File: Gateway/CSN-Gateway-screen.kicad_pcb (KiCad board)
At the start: 2 copper layers, 32 x 58 mm, 27 parts, among them IC2 FT232RL, P1 USB_MINI, P2 CONN_01X12, P4 CONN_OLED_SCREEN, SW1 SW_PUSH, SW2 SW_PUSH

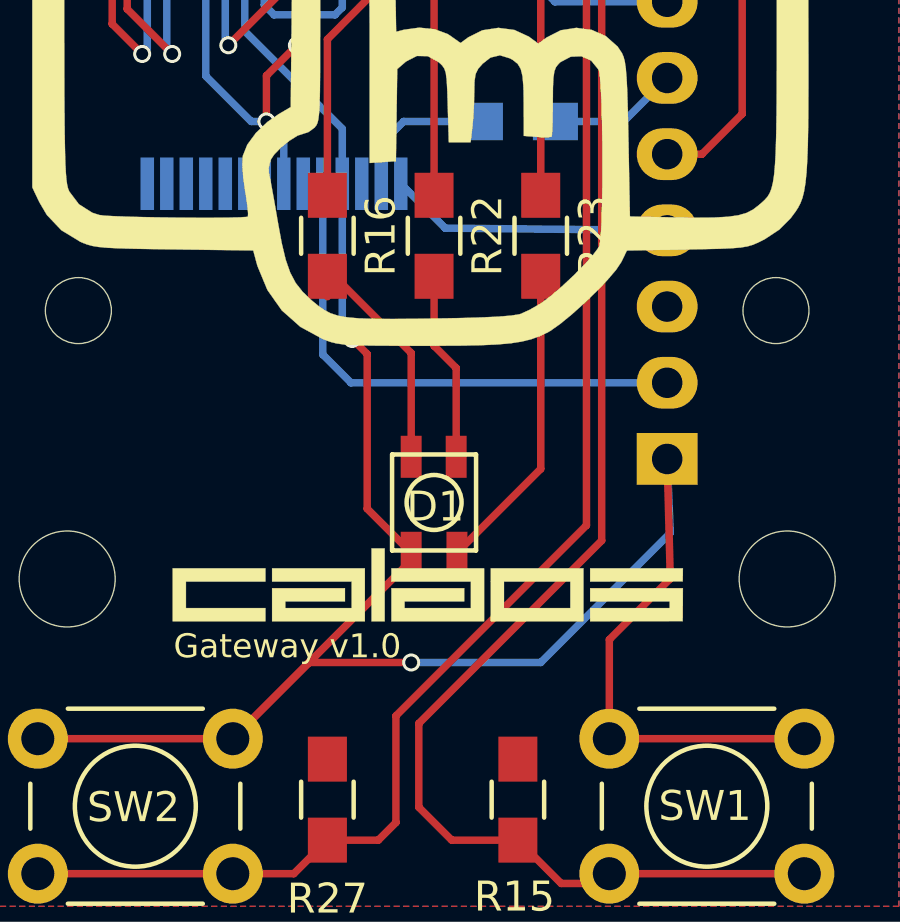
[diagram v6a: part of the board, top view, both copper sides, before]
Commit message: fix wrong footprints
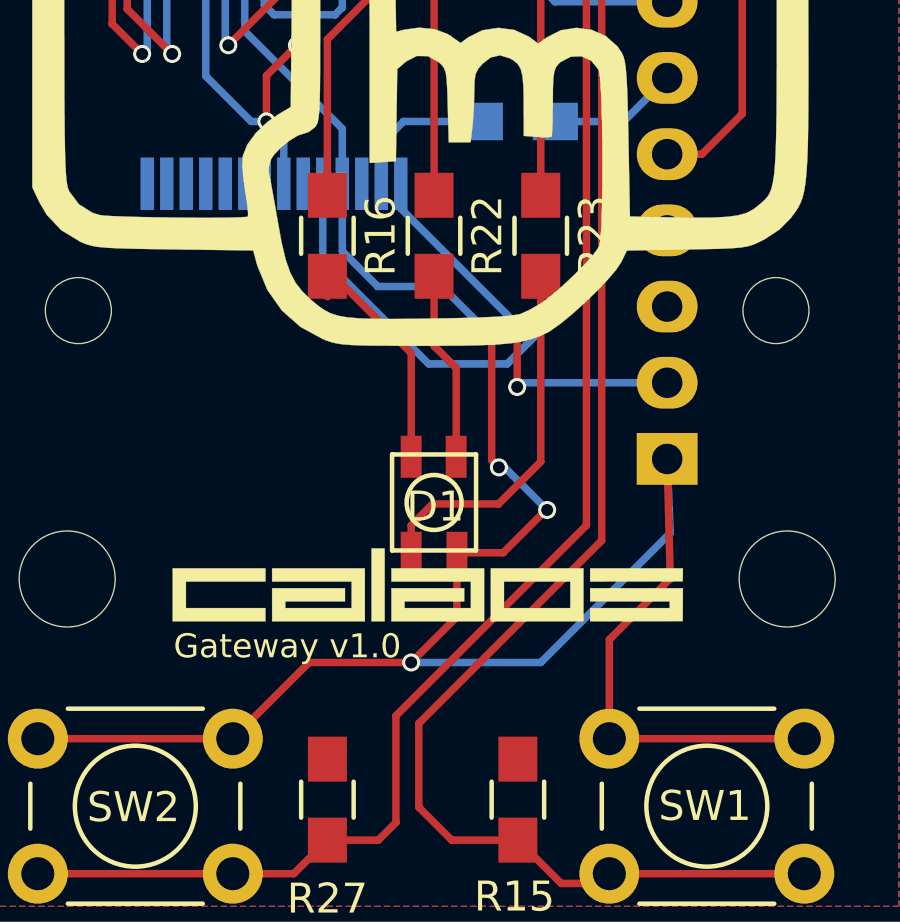
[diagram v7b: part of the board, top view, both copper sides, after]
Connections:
- D1 pad 2: VCC -> Net-(D1-Pad2)
- D1 pad 3: Net-(D1-Pad3) -> VCC
- IC2 pad 10: (no net) -> Net-(IC2-Pad10)
- IC2 pad 11: (no net) -> Net-(IC2-Pad11)
- IC2 pad 12: (no net) -> Net-(IC2-Pad12)
- IC2 pad 13: (no net) -> Net-(IC2-Pad13)
- IC2 pad 14: (no net) -> Net-(IC2-Pad14)
- IC2 pad 17: (no net) -> Net-(IC2-Pad17)
- IC2 pad 22: (no net) -> Net-(IC2-Pad22)
- IC2 pad 23: (no net) -> Net-(IC2-Pad23)
- IC2 pad 27: (no net) -> Net-(IC2-Pad27)
- IC2 pad 28: (no net) -> Net-(IC2-Pad28)
- IC2 pad 3: (no net) -> Net-(IC2-Pad3)
- IC2 pad 6: (no net) -> Net-(IC2-Pad6)
- IC2 pad 9: (no net) -> Net-(IC2-Pad9)
- P1 pad 4: (no net) -> Net-(P1-Pad4)
- P2 pad 2: TXO -> RXI
- P2 pad 4: RXI -> TXO
- R23 pad 2: Net-(D1-Pad3) -> Net-(D1-Pad2)
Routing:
- net Net-(D1-Pad2): track 0.00 -> 12.5 mm
- net Net-(D1-Pad3): track 10.4 -> 0.00 mm
- net RXI: track 9.49 -> 13.5 mm, vias 0 -> 2
- net VCC: track 88.5 -> 89.5 mm, vias 2 -> 4
